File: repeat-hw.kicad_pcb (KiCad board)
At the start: 6 copper layers, 50 x 50 mm, 159 parts, among them J1 USB_C_Receptacle_USB2.0, J2 ARJM11C7-114-BA-EW2, J3 ANT2, J4 Programming header, T1 FA2805, U1 nRF5340-QKxx, U10 USBLC6-2SC6, U11 USBLC6-2SC6, U12 MX25R3235FZNxx0, U2 USBLC6-2SC6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

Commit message: Finalized for production
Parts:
- removed the J2 at (166.5, 93.8)
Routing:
- net Net-(C61-Pad2): track 2.50 -> 18.7 mm
- net Net-(FB6-Pad2): track 5.28 -> 15.0 mm, vias 0 -> 1
- net GND: track 49.1 -> 54.7 mm, vias 268 -> 266
- net /W5100 + PoE/CON_RD+: track 9.53 -> 14.1 mm
- net /W5100 + PoE/CON_RD-: track 9.36 -> 14.0 mm
- net /W5100 + PoE/ESD_RD+: track 11.6 -> 7.08 mm
- net /W5100 + PoE/ESD_RD-: track 11.4 -> 7.24 mm
- net Earth: track 8.87 -> 9.51 mm
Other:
- outline, holes or cut-outs redrawn
- board text added: "JLCJLCJLCJLC"

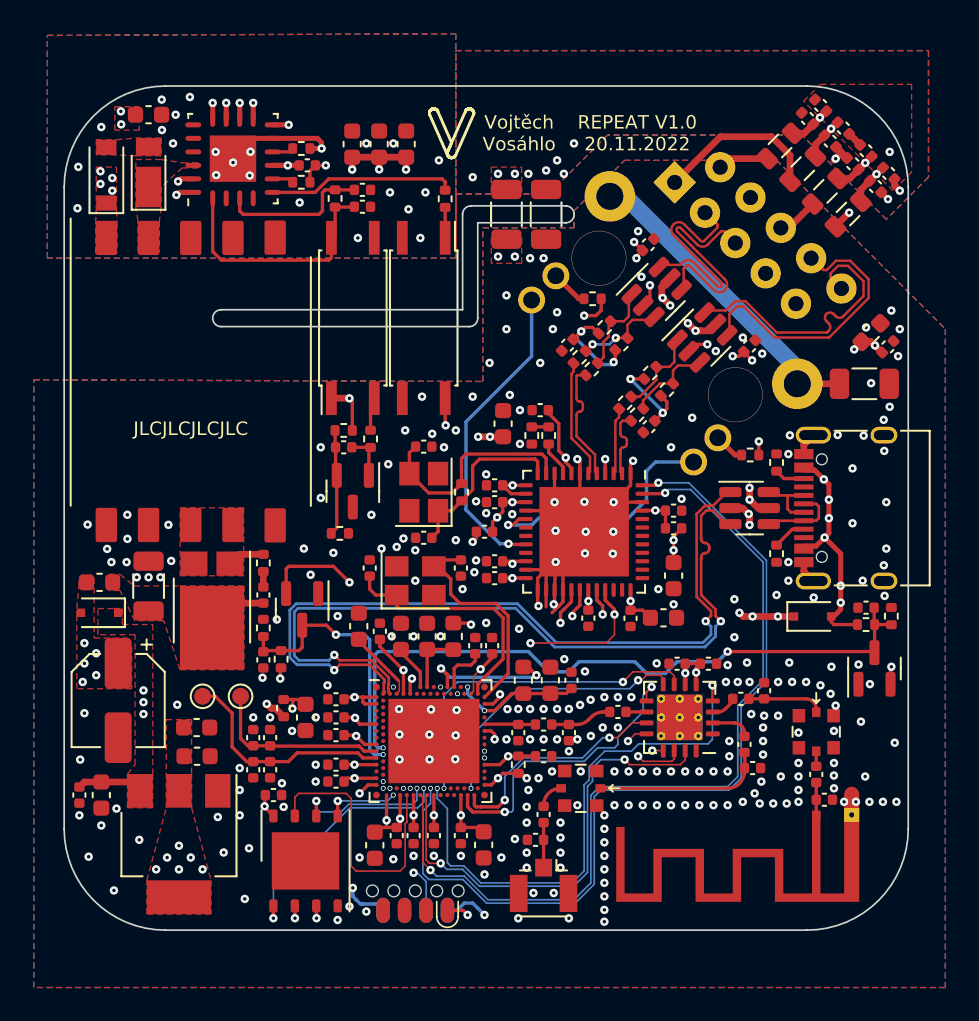
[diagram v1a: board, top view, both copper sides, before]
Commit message: Changed via to copper clearance to correct value
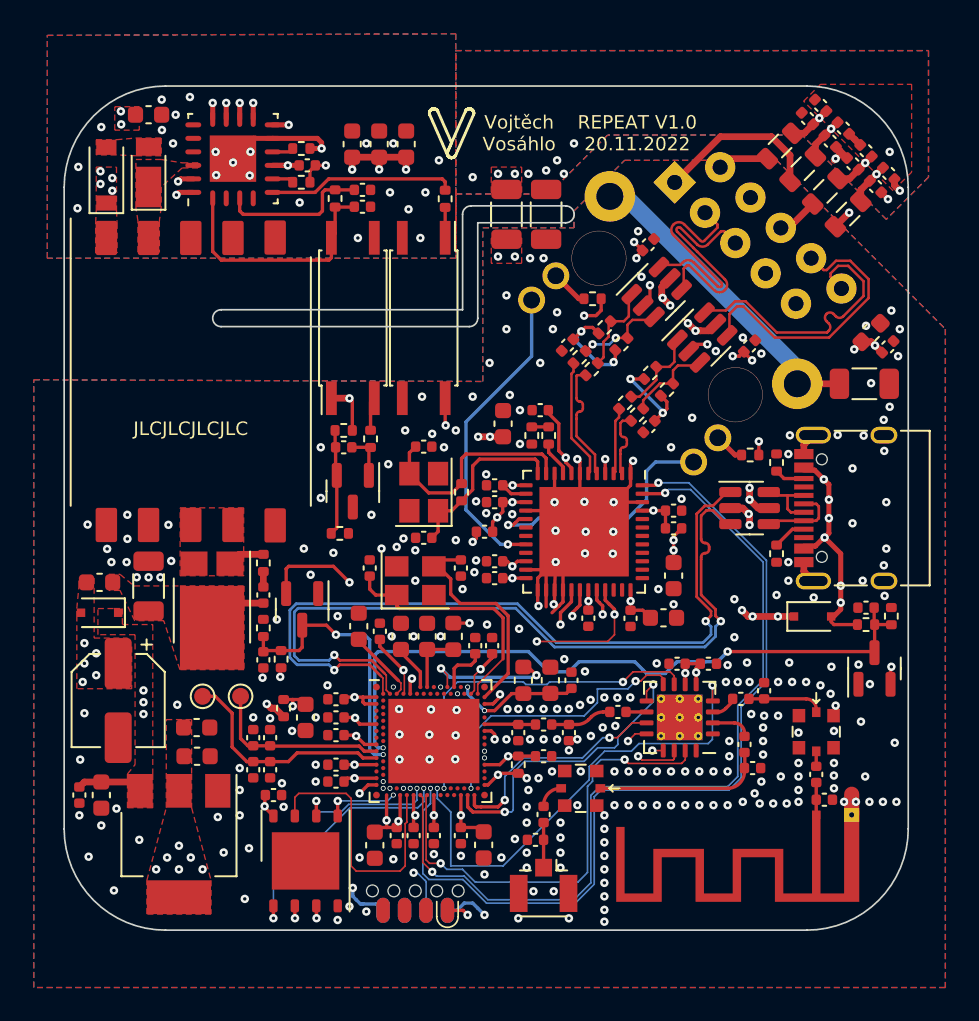
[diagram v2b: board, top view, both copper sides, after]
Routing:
- net /FEM_MODE: track 31.9 -> 28.1 mm
